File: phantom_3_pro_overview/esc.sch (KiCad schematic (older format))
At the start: 0 parts

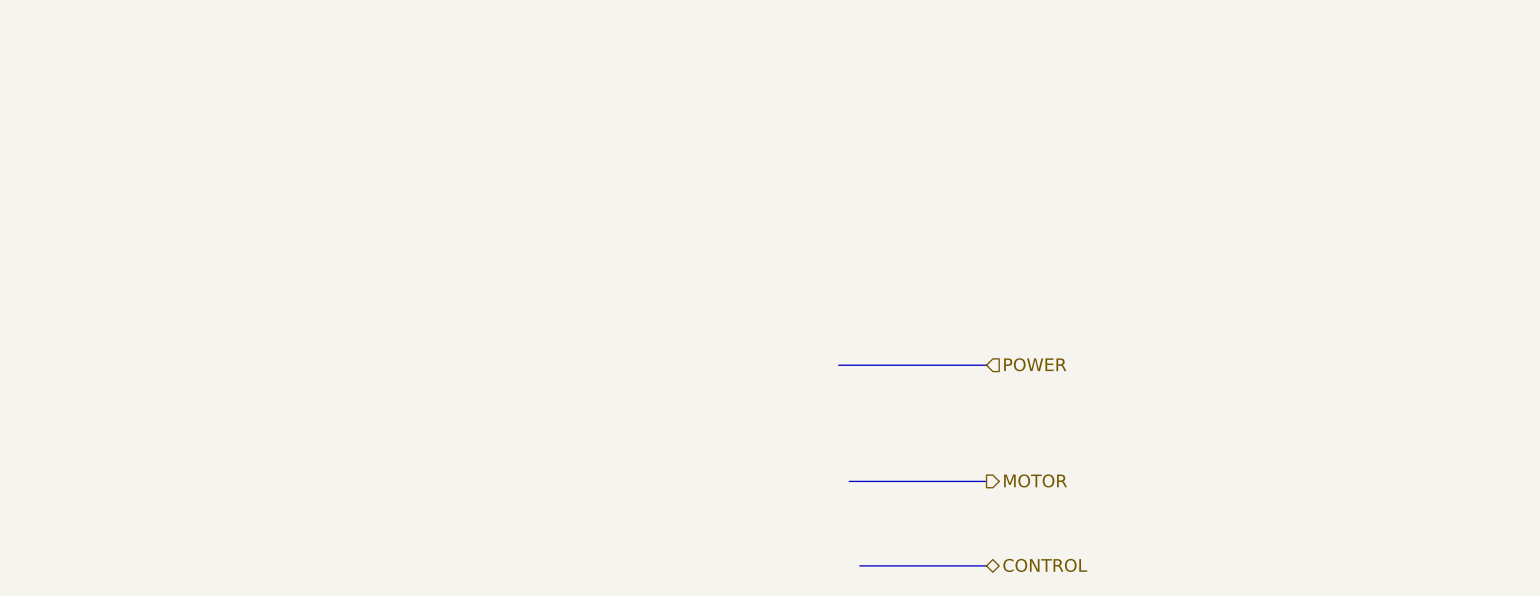
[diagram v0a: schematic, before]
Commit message: Overview: Conceptual schematics of some components.
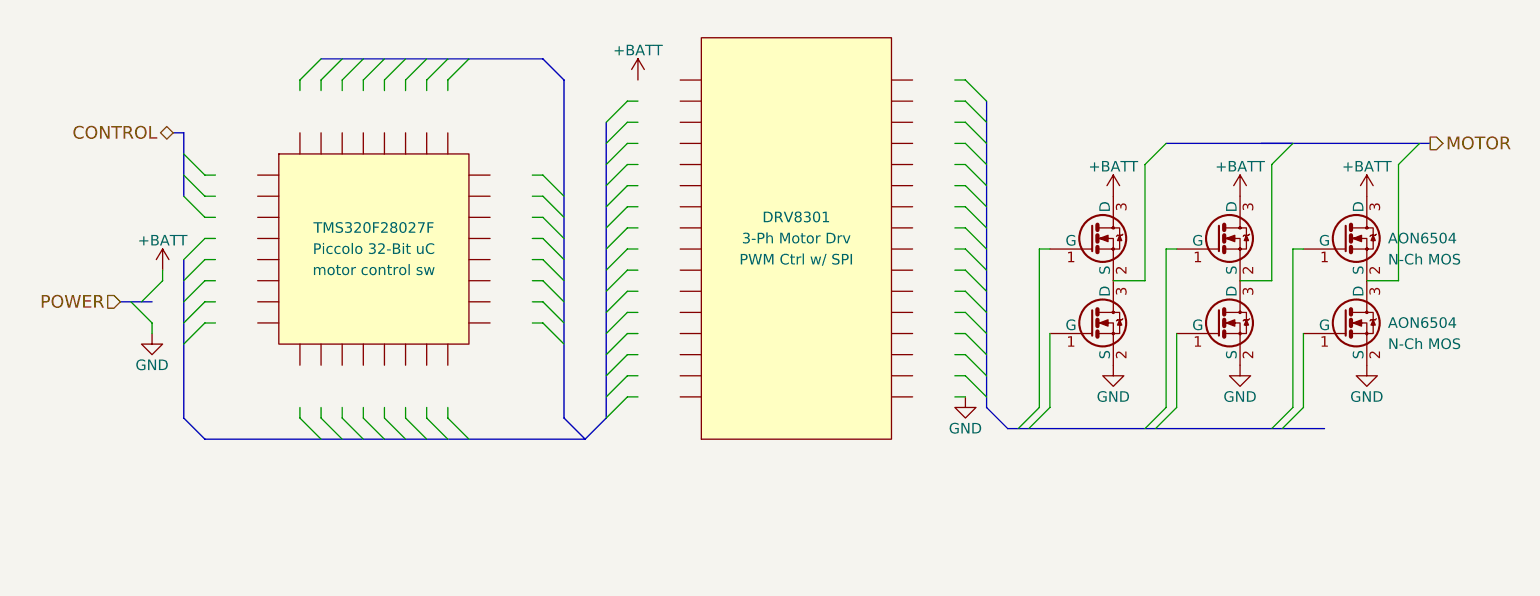
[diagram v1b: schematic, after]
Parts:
- added Q? (x6): AON6504, TO_SOT_Packages_SMD:SOT-23, symbol BSS138
- added U?: DRV8301, PWM Ctrl w/ SPI, symbol IC_DIL32
- added U?: TMS320F28027F, motor control sw, symbol IC_PQFP32
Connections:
- net labels added: +BATT, GND
- wire segments 0 -> 80

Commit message: Overview: Added OFDM board.
Besides drawing the OFDM, components were updated.
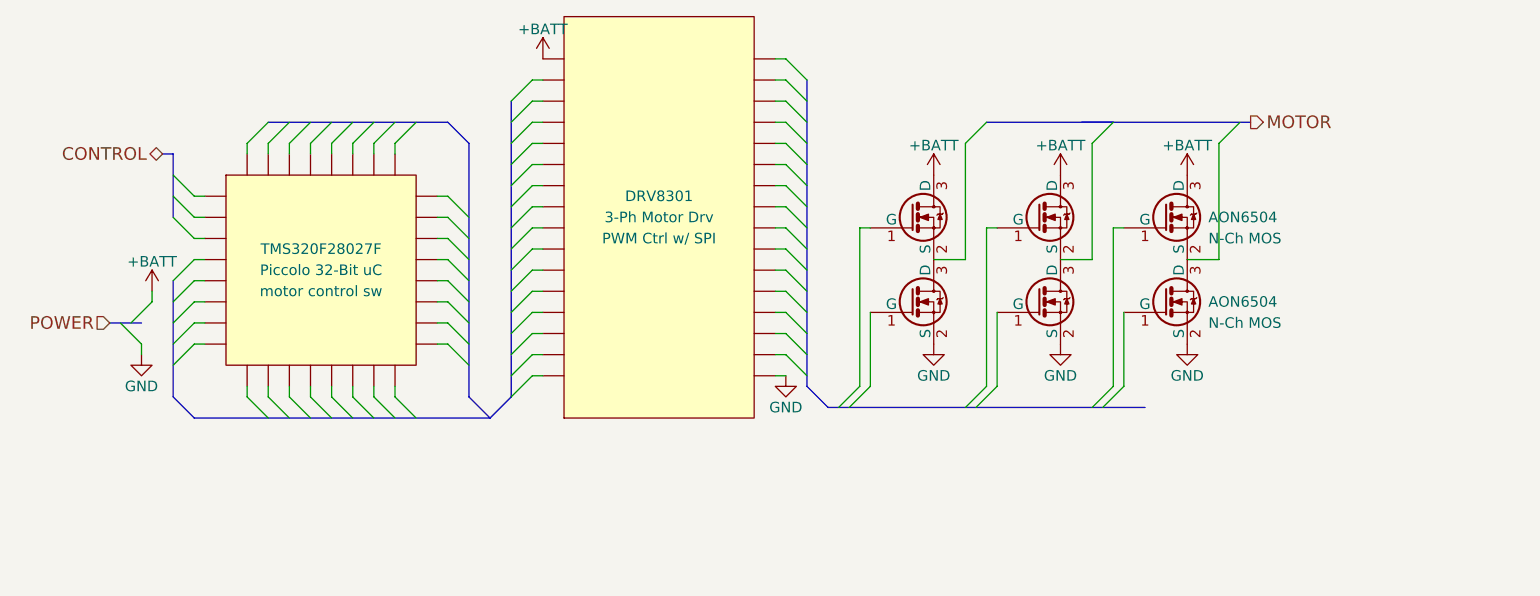
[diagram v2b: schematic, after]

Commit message: Overview: Upgraded to KiCAD 5.0.1.
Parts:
- Q? (x6): symbol BSS138 -> phantom_3_pro_overview-rescue:BSS138
- U?: symbol IC_DIL32 -> ic_dil_generic:IC_DIL32
- U?: symbol IC_PQFP32 -> ic_dil_generic:IC_PQFP32
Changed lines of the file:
@@
-EESchema Schematic File Version 2
-LIBS:power
-LIBS:device
-LIBS:transistors
-LIBS:conn
-LIBS:linear
-LIBS:regul
-LIBS:74xx
-LIBS:cmos4000
-LIBS:adc-dac
-LIBS:memory
-LIBS:xilinx
-LIBS:microcontrollers
-LIBS:dsp
-LIBS:microchip
-LIBS:analog_switches
-LIBS:motorola
-LIBS:texas
-LIBS:intel
-LIBS:audio
-LIBS:interface
-LIBS:digital-audio
-LIBS:philips
-LIBS:display
-LIBS:cypress
-LIBS:siliconi
-LIBS:opto
-LIBS:atmel
-LIBS:contrib
-LIBS:valves
-LIBS:motors
-LIBS:ic_dil_generic
-LIBS:sensors
-LIBS:u-blox
-LIBS:amplifiers
-LIBS:transistors-switches
-LIBS:transistors-power
-LIBS:sensors-v2
-LIBS:regul-v2
+EESchema Schematic File Version 4
 LIBS:phantom_3_pro_overview-cache
-EELAYER 25 0
+EELAYER 26 0
 EELAYER END
 $Descr User 7402 4725
@@
 CONTROL
 $Comp
-L IC_DIL32 U?
+L ic_dil_generic:IC_DIL32 U?
 U 1 1 596D4343
 P 3600 1600
@@
 $EndComp
 $Comp
-L BSS138 Q?
+L phantom_3_pro_overview-rescue:BSS138 Q?
 U 1 1 596D44EF
 P 4800 1600
 AR Path="/596D582B/596D44EF" Ref="Q?"  Part="1"
 AR Path="/596D6DC3/596D44EF" Ref="Q?"  Part="1"
+AR Path="/596D44EF" Ref="Q?"  Part="1"
 F 0 "Q?" H 5000 1675 50  0001 L CNN
 F 1 "AON6504" H 5000 1600 50  0001 L CNN
@@
 	1100 2100 1200 2000
 $Comp
-L GND #PWR?
+L power:GND #PWR?
 U 1 1 596D4634
 P 1150 2250
@@
 $EndComp
 $Comp
-L +BATT #PWR?
+L power:+BATT #PWR?
 U 1 1 596D464C
 P 1200 1950
@@
 $EndComp
 $Comp
-L BSS138 Q?
+L phantom_3_pro_overview-rescue:BSS138 Q?
 U 1 1 596D493A
 P 4800 2000
 AR Path="/596D582B/596D493A" Ref="Q?"  Part="1"
 AR Path="/596D6DC3/596D493A" Ref="Q?"  Part="1"
+AR Path="/596D493A" Ref="Q?"  Part="1"
 F 0 "Q?" H 5000 2075 50  0001 L CNN
 F 1 "AON6504" H 5000 2000 50  0001 L CNN
@@
 $EndComp
 $Comp
-L +BATT #PWR?
+L power:+BATT #PWR?
 U 1 1 596D495A
 P 4900 1400
@@
 $EndComp
 $Comp
-L GND #PWR?
+L power:GND #PWR?
 U 1 1 596D496E
 P 4900 2200
@@
 $EndComp
 $Comp
-L BSS138 Q?
+L phantom_3_pro_overview-rescue:BSS138 Q?
 U 1 1 596D4994
 P 5400 1600
 AR Path="/596D582B/596D4994" Ref="Q?"  Part="1"
 AR Path="/596D6DC3/596D4994" Ref="Q?"  Part="1"
+AR Path="/596D4994" Ref="Q?"  Part="1"
 F 0 "Q?" H 5600 1675 50  0001 L CNN
 F 1 "AON6504" H 5600 1600 50  0001 L CNN
@@
 $EndComp
 $Comp
-L BSS138 Q?
+L phantom_3_pro_overview-rescue:BSS138 Q?
 U 1 1 596D499A
 P 5400 2000
 AR Path="/596D582B/596D499A" Ref="Q?"  Part="1"
 AR Path="/596D6DC3/596D499A" Ref="Q?"  Part="1"
+AR Path="/596D499A" Ref="Q?"  Part="1"
 F 0 "Q?" H 5600 2075 50  0001 L CNN
 F 1 "AON6504" H 5600 2000 50  0001 L CNN
@@
 $EndComp
 $Comp
-L +BATT #PWR?
+L power:+BATT #PWR?
 U 1 1 596D49A0
 P 5500 1400
@@
 $EndComp
 $Comp
-L GND #PWR?
+L power:GND #PWR?
 U 1 1 596D49A6
 P 5500 2200
@@
 $EndComp
 $Comp
-L BSS138 Q?
+L phantom_3_pro_overview-rescue:BSS138 Q?
 U 1 1 596D49AC
 P 6000 1600
 AR Path="/596D582B/596D49AC" Ref="Q?"  Part="1"
 AR Path="/596D6DC3/596D49AC" Ref="Q?"  Part="1"
+AR Path="/596D49AC" Ref="Q?"  Part="1"
 F 0 "Q?" H 6200 1675 50  0001 L CNN
 F 1 "AON6504" H 6200 1600 50  0000 L CNN
@@
 $EndComp
 $Comp
-L BSS138 Q?
+L phantom_3_pro_overview-rescue:BSS138 Q?
 U 1 1 596D49B2
 P 6000 2000
 AR Path="/596D582B/596D49B2" Ref="Q?"  Part="1"
 AR Path="/596D6DC3/596D49B2" Ref="Q?"  Part="1"
+AR Path="/596D49B2" Ref="Q?"  Part="1"
 F 0 "Q?" H 6200 2075 50  0001 L CNN
 F 1 "AON6504" H 6200 2000 50  0000 L CNN
@@
 $EndComp
 $Comp
-L +BATT #PWR?
+L power:+BATT #PWR?
 U 1 1 596D49B8
 P 6100 1400
@@
 $EndComp
 $Comp
-L GND #PWR?
+L power:GND #PWR?
 U 1 1 596D49BE
 P 6100 2200
@@
 	4150 950  4200 950
 $Comp
-L GND #PWR?
+L power:GND #PWR?
 U 1 1 596D4DE1
 P 4200 2350
@@
 $EndComp
 $Comp
-L +BATT #PWR?
+L power:+BATT #PWR?
 U 1 1 596D4DF5
 P 3050 850
@@
 Wire Wire Line
 	1450 2200 1400 2200
-Wire Bus Line
-	1000 2100 1150 2100
-Wire Bus Line
-	4300 950  4300 2400
 Entry Bus Bus
 	1300 2450 1400 2550
@@
 Entry Bus Bus
 	4300 2400 4400 2500
-Wire Bus Line
-	4400 2500 5900 2500
-Wire Bus Line
-	5150 1150 5750 1150
-Wire Bus Line
-	5600 1150 6400 1150
 Wire Wire Line
 	1200 1950 1200 2000
@@
 	1150 2200 1150 2250
 $Comp
-L IC_PQFP32 U?
+L ic_dil_generic:IC_PQFP32 U?
 U 1 1 596DC297
 P 2000 1850
@@
 	1450 1800 1400 1800
 Wire Bus Line
-	1300 1600 1300 1300
-Wire Bus Line
-	2900 2450 2900 1050
+	1000 2100 1150 2100
+Wire Bus Line
+	1300 1300 1300 1600
+Wire Bus Line
+	5150 1150 6400 1150
+Wire Bus Line
+	1300 1900 1300 2450
+Wire Bus Line
+	4400 2500 5900 2500
 Wire Bus Line
 	1400 2550 2800 2550
 Wire Bus Line
-	2600 1150 1750 1150
+	1750 1150 2600 1150
 Wire Bus Line
 	2700 1250 2700 2450
 Wire Bus Line
-	1300 1900 1300 2450
+	4300 950  4300 2400
+Wire Bus Line
+	2900 1050 2900 2450
 $EndSCHEMATC

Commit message: All: Finished updating to KiCad 5.0.1.
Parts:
- Q? (x6): symbol phantom_3_pro_overview-rescue:BSS138 -> Transistor_FET-v2:AON6504
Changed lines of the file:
@@
 $EndComp
 $Comp
-L phantom_3_pro_overview-rescue:BSS138 Q?
+L Transistor_FET-v2:AON6504 Q?
 U 1 1 596D44EF
 P 4800 1600
@@
 $EndComp
 $Comp
-L phantom_3_pro_overview-rescue:BSS138 Q?
+L Transistor_FET-v2:AON6504 Q?
 U 1 1 596D493A
 P 4800 2000
@@
 $EndComp
 $Comp
-L phantom_3_pro_overview-rescue:BSS138 Q?
+L Transistor_FET-v2:AON6504 Q?
 U 1 1 596D4994
 P 5400 1600
@@
 $EndComp
 $Comp
-L phantom_3_pro_overview-rescue:BSS138 Q?
+L Transistor_FET-v2:AON6504 Q?
 U 1 1 596D499A
 P 5400 2000
@@
 $EndComp
 $Comp
-L phantom_3_pro_overview-rescue:BSS138 Q?
+L Transistor_FET-v2:AON6504 Q?
 U 1 1 596D49AC
 P 6000 1600
@@
 $EndComp
 $Comp
-L phantom_3_pro_overview-rescue:BSS138 Q?
+L Transistor_FET-v2:AON6504 Q?
 U 1 1 596D49B2
 P 6000 2000
@@
 Wire Wire Line
 	1450 1800 1400 1800
+Connection ~ 4900 1800
 Wire Bus Line
 	1000 2100 1150 2100
 Wire Bus Line
+	5150 1150 6400 1150
+Wire Bus Line
 	1300 1300 1300 1600
 Wire Bus Line
-	5150 1150 6400 1150
-Wire Bus Line
 	1300 1900 1300 2450
